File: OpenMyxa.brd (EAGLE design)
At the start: 58 x 58 mm, 106 parts, among them CON1 USB, CON2 PINHEAD_1X01-2, CON3 CON-4P-TABS-STRAIGHT, CON4 CON-4P-TABS-STRAIGHT, CON5 CON-4P-TABS-STRAIGHT, CON6 CON-4P-TABS-STRAIGHT, CON7 CON-4P-TABS-STRAIGHT, CON8 CON-6P, CON9 PINHEAD_1X01-2, IC1 TPD3S014DBVR-SOT23-6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

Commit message: Migration to updated mitochondrik library
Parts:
- MODULE2: value MITOHONDRIQUE-TH -> MITOHONDRIQUE_V0.2-TH
- moved C2 1.00 mm to (40.2, 8.60), flipped to the top
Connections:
- net BEC_ENABLE_OUT: now also MODULE2.21; no longer MODULE2.24
- net CAN1_LED: now also MODULE2.33; no longer MODULE2.36
- net CAN1_RX: now also MODULE2.38; no longer MODULE2.41
- net CAN1_TX: now also MODULE2.39; no longer MODULE2.42
- net CAN2_LED: now also MODULE2.34; no longer MODULE2.37
- net CAN2_RX: now also MODULE2.36; no longer MODULE2.39
- net CAN2_TX: now also MODULE2.37; no longer MODULE2.40
- net GAIN_OUT: now also MODULE2.22; no longer MODULE2.25
- net GATE_ENABLE_OUT: now also MODULE2.23; no longer MODULE2.26
- net GND: now also MODULE2.41; no longer MODULE2.2
- net GPIO1: now also MODULE2.25; no longer MODULE2.28
- net GPIO2: now also MODULE2.24; no longer MODULE2.27
- net LED_BLUE: now also MODULE2.29; no longer MODULE2.32
- net LED_GREEN: now also MODULE2.28; no longer MODULE2.31
- net LED_RED: now also MODULE2.27; no longer MODULE2.30
- net N$18: now also MODULE2.26; no longer MODULE2.29
- net N$5: now also MODULE2.30; no longer MODULE2.33
- net N$51: now also MODULE2.31; no longer MODULE2.34
- net N$55: now also MODULE2.32; no longer MODULE2.35
- net PHASE_A: now also MODULE2.2; no longer MODULE2.5
- net PHASE_A_CURRENT_SHUNT_N: now also MODULE2.13; no longer MODULE2.16
- net PHASE_A_CURRENT_SHUNT_P: now also MODULE2.14; no longer MODULE2.17
- net PHASE_A_GATE_HIGH: now also MODULE2.1; no longer MODULE2.4
- net PHASE_A_GATE_LOW: now also MODULE2.3; no longer MODULE2.6
- net PHASE_A_GND: now also MODULE2.4; no longer MODULE2.7
- net PHASE_B: now also MODULE2.6; no longer MODULE2.9
- net PHASE_B_CURRENT_SHUNT_N: now also MODULE2.15; no longer MODULE2.18
- net PHASE_B_CURRENT_SHUNT_P: now also MODULE2.16; no longer MODULE2.19
- net PHASE_B_GATE_HIGH: now also MODULE2.5; no longer MODULE2.8
- net PHASE_B_GATE_LOW: now also MODULE2.7; no longer MODULE2.10
- net PHASE_B_GND: now also MODULE2.8; no longer MODULE2.11
- net PHASE_C: now also MODULE2.10; no longer MODULE2.13
- net PHASE_C_GATE_HIGH: now also MODULE2.9; no longer MODULE2.12
- net PHASE_C_GATE_LOW: now also MODULE2.11; no longer MODULE2.14
- net PHASE_C_GND: now also MODULE2.12; no longer MODULE2.15
- net TEMPERATURE_SENSOR: now also MODULE2.17; no longer MODULE2.20
- net UART_RX: now also MODULE2.20; no longer MODULE2.23
- net UART_TX: now also MODULE2.19; no longer MODULE2.22
- net VDC: now also MODULE2.42; no longer MODULE2.3
- net VDD_5V: now also MODULE2.40; no longer MODULE2.1
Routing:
- net VDC: track 9.14 -> 7.70 mm
- net PHASE_B_GATE_LOW: track 3.75 -> 2.65 mm
- net GPIO1: track 28.8 -> 29.8 mm
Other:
- board text removed: "+"

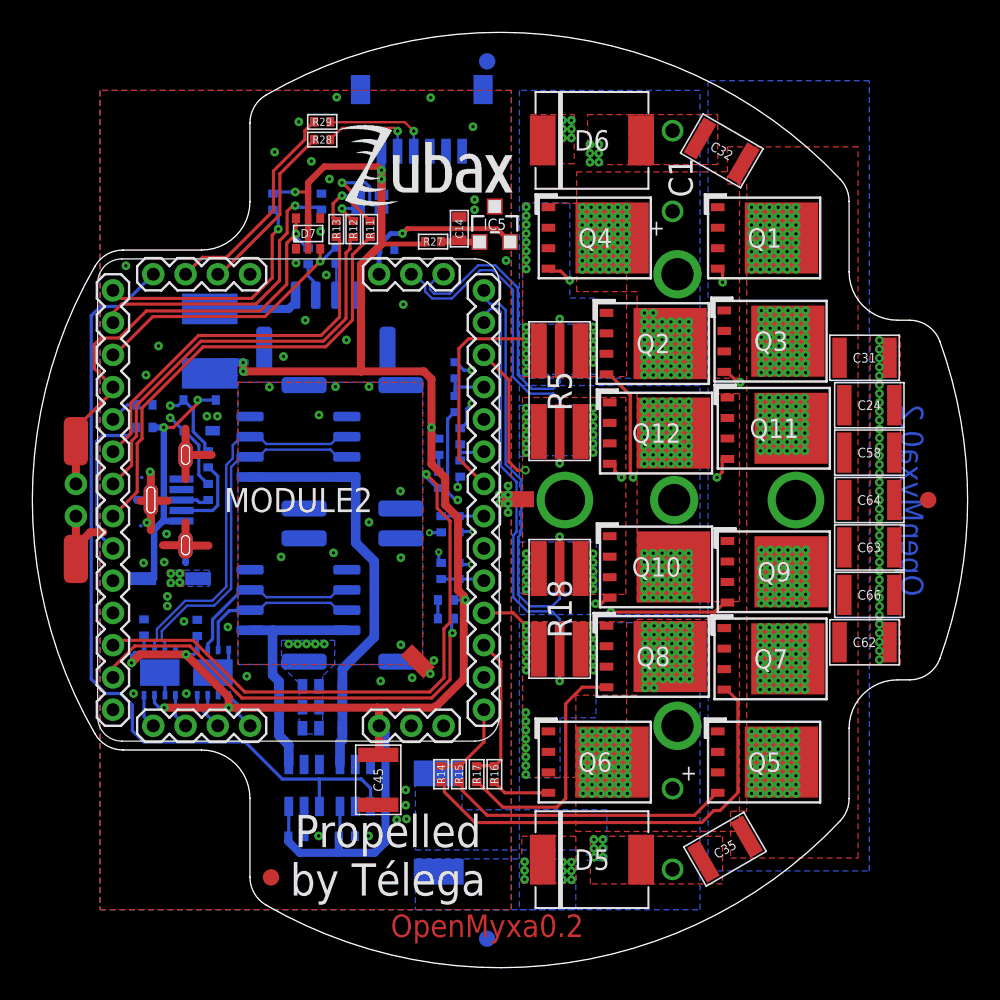
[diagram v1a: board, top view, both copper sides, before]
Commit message: component selection updates
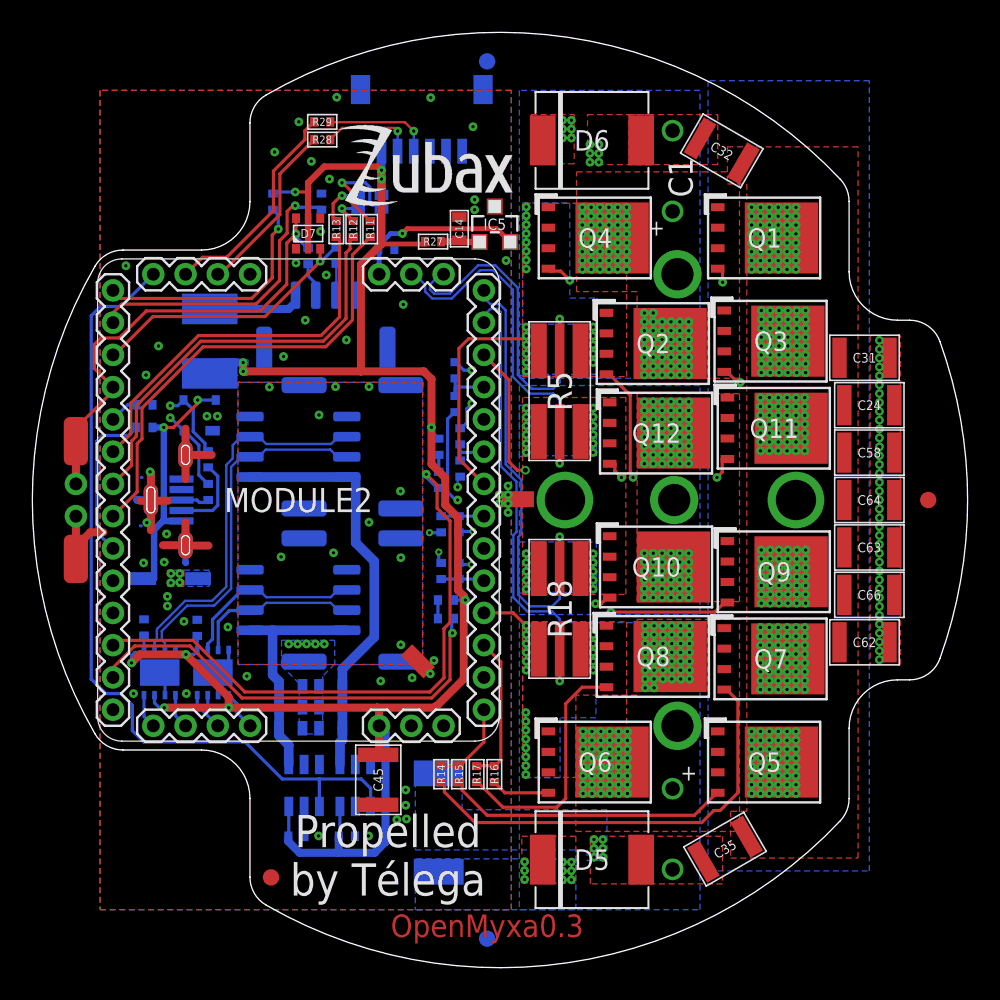
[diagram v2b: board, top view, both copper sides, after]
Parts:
- C1, C2: value 220uF 63V -> 330uF 63V
- D1, D5, D6: value TPSMC62A -> SMCJ51A
- R5: value 1 mOhms -> 1.5 mOhms
- R7: value 1K -> 1K5; device R_digikey:R0402 -> rc:R0402
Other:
- board text added: "OpenMyxa0.3"
- board text removed: "OpenMyxa0.2"
